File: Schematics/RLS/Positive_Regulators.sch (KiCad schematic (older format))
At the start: 4 parts

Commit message: Updated Regulator Circuits and Fixed Velleman Gain
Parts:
- removed U? (x2): AD5293, symbol AD5293
- added C21, C23, C25, C27, C29, C31, C? (x2): 10uF, symbol CP1
- added C22, C24, C26, C28, C30, C32: 0.1uF, symbol C
- added C33, C35: 1uF, symbol CP1
- added R?: 4.7K, symbol R
- added R?: 1K, symbol R
- added U8, U9: AD5293, symbol AD5293-RESCUE-RLS
- gave numbers to parts that had none: 2
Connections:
- net labels added: +15V, +5V, -15V, -15v, -V2, -V2_SHDN, AGND, MOSI, P_POT_CE, SCLK
- wire segments 0 -> 76
- no-connect marks 0 -> 3
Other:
- moved on the sheet: U10, U11

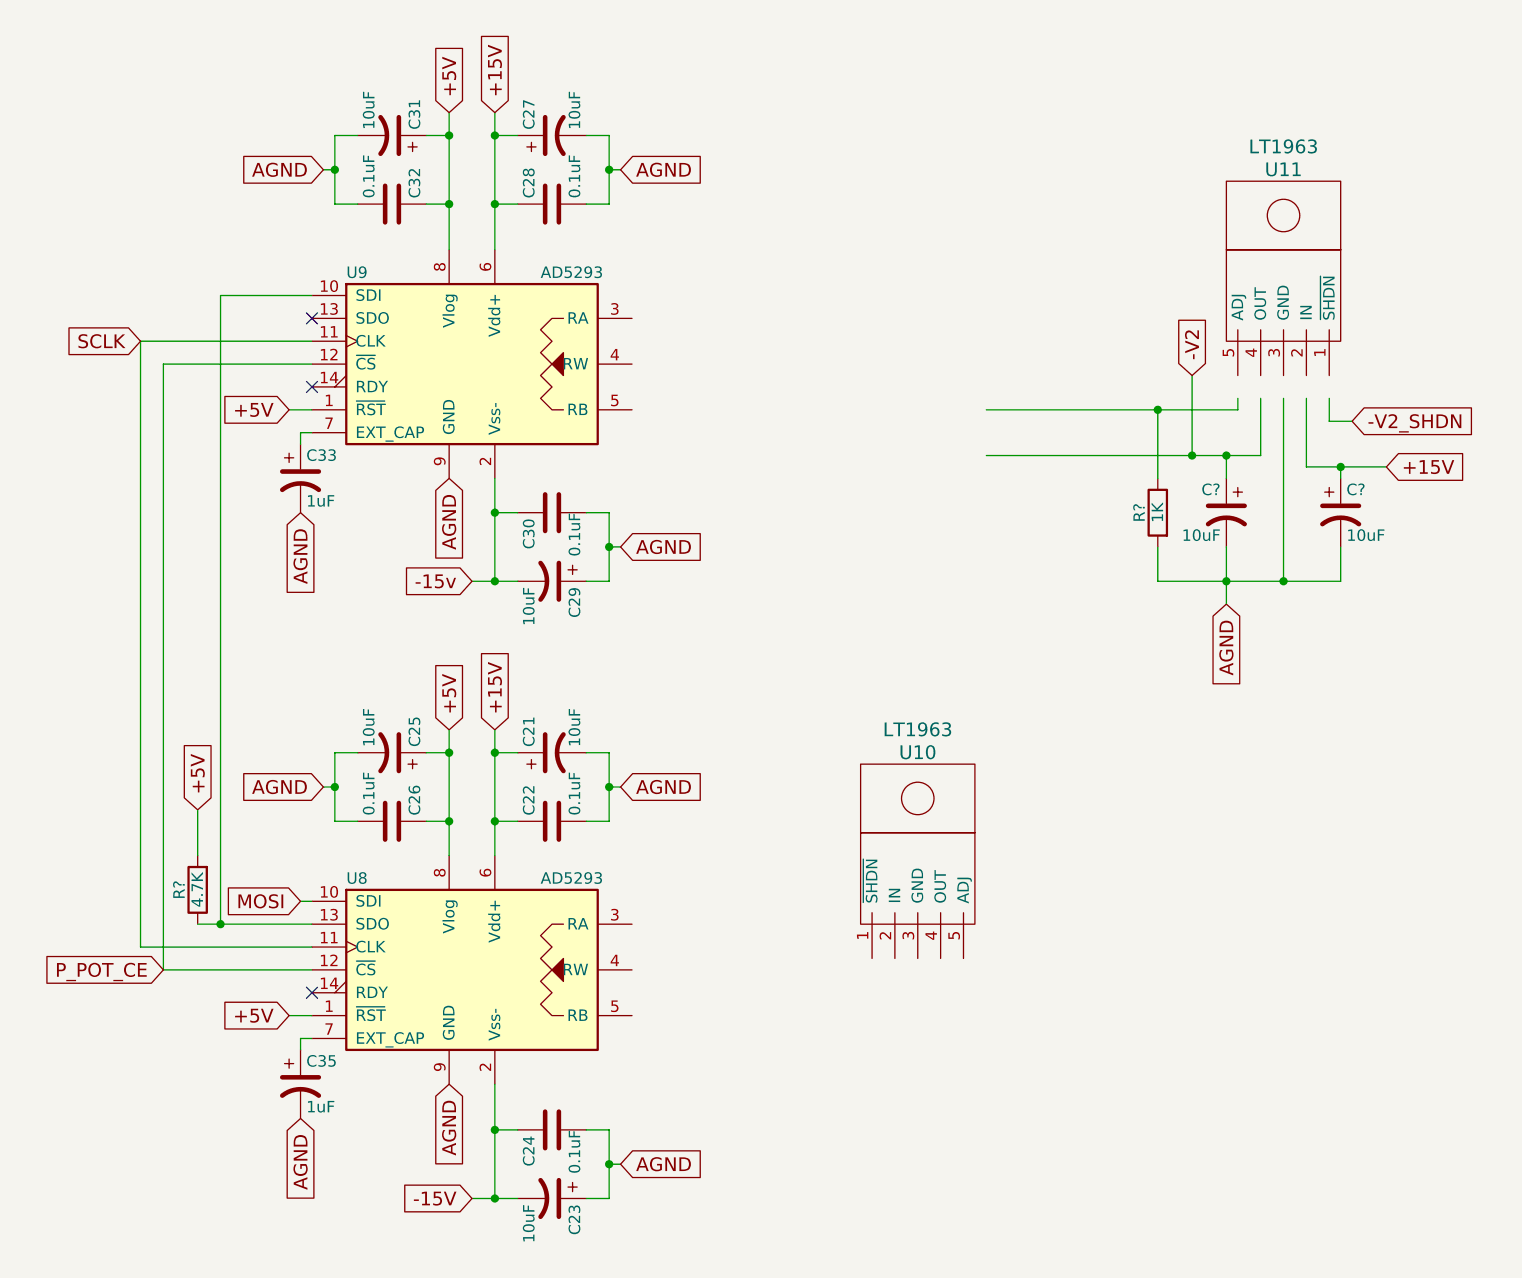
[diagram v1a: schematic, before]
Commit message: Updated Schematic (Almost Done)
Finished both variable regulator circuits, added connectors for LAs, added +/- 5 regulated circuit for DB +/- 5V (needs to be tested before PCB implementation), various renaming and labeling
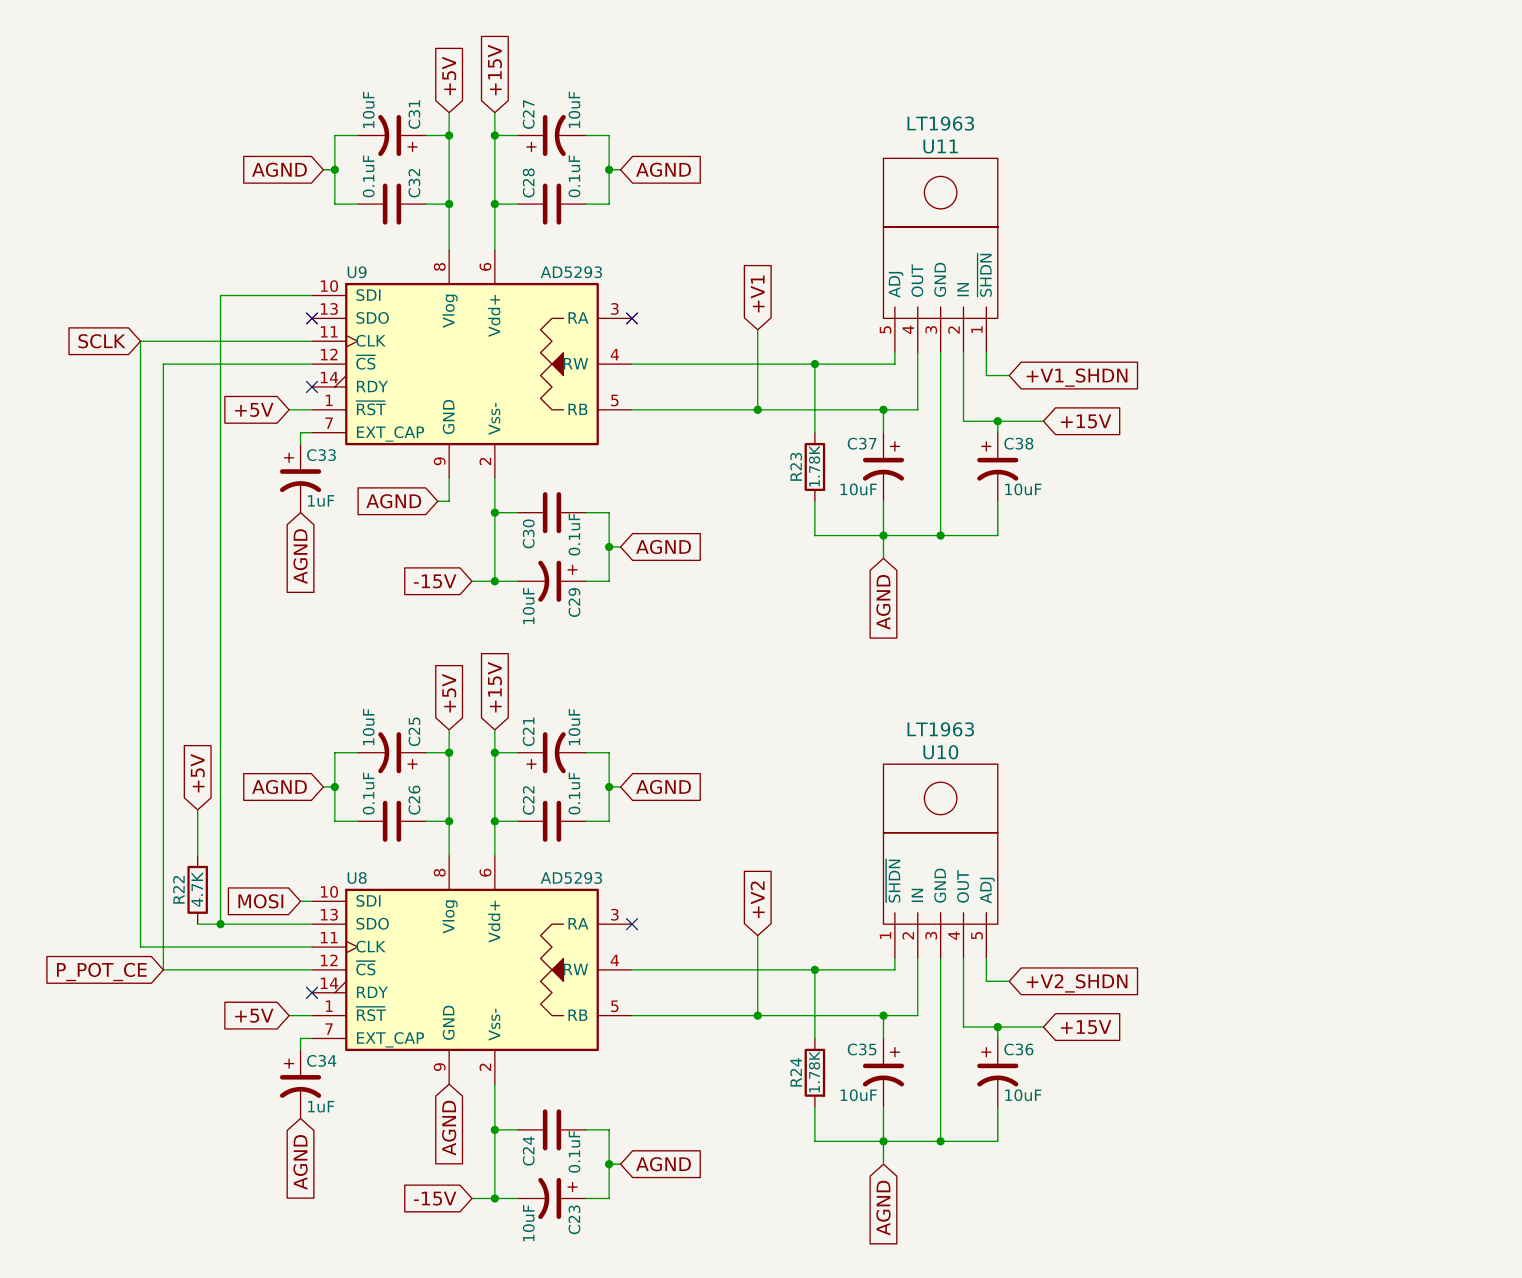
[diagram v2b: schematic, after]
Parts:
- added C35, C36: 10uF, symbol CP1
- added R24: 1.78K, symbol R
- R23: renamed from R?; value 1K -> 1.78K
- gave numbers to parts that had none: 3
- renumbered C35 to C34
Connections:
- net labels added: +V1, +V1_SHDN, +V2, +V2_SHDN
- net labels removed: -15v, -V2, -V2_SHDN
- wire segments 76 -> 95
- no-connect marks 3 -> 5
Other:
- moved on the sheet: C37, C38, R23, U10, U11

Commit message: Most Footprints Added
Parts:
- C21, C23, C25, C27, C29, C31, C33, C34, C35, C36, C37, C38: footprint (none) -> Capacitors_SMD:CP_Elec_4x5.3
- C22, C24, C26, C28, C30, C32: footprint (none) -> Capacitors_SMD:C_0603_HandSoldering
- R22: footprint (none) -> Resistors_SMD:R_0805_HandSoldering
- R23, R24: footprint (none) -> Resistors_SMD:R_1206_HandSoldering
- U10, U11: footprint (none) -> TO_SOT_Packages_THT:TO-220-5_Pentawatt_Multiwatt-5_Vertical_StaggeredType1
- U8, U9: footprint (none) -> SMD_Packages:SSOP-14
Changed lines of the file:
@@
 F 0 "U11" H 5250 2700 60  0000 C CNN
 F 1 "LT1963" H 5250 2800 60  0000 C CNN
-F 2 "" H 5250 2700 60  0001 C CNN
+F 2 "TO_SOT_Packages_THT:TO-220-5_Pentawatt_Multiwatt-5_Vertical_StaggeredType1" H 5250 2700 60  0001 C CNN
 F 3 "" H 5250 2700 60  0001 C CNN
 	1    5200 2200
@@
 F 0 "U10" H 5150 5350 60  0000 C CNN
 F 1 "LT1963" H 5150 5450 60  0000 C CNN
-F 2 "" H 5150 5350 60  0001 C CNN
+F 2 "TO_SOT_Packages_THT:TO-220-5_Pentawatt_Multiwatt-5_Vertical_StaggeredType1" H 5150 5350 60  0001 C CNN
 F 3 "" H 5150 5350 60  0001 C CNN
 	1    5100 4850
@@
 F 0 "U8" H 2550 5700 50  0000 L CNN
 F 1 "AD5293" H 3400 5700 50  0000 L CNN
-F 2 "" H 3100 5300 50  0001 C CNN
+F 2 "SMD_Packages:SSOP-14" H 3100 5300 50  0001 C CNN
 F 3 "" H 3100 5300 50  0001 C CNN
 	1    3100 5300
@@
 F 0 "U9" H 2550 3050 50  0000 L CNN
 F 1 "AD5293" H 3400 3050 50  0000 L CNN
-F 2 "" H 3100 2650 50  0001 C CNN
+F 2 "SMD_Packages:SSOP-14" H 3100 2650 50  0001 C CNN
 F 3 "" H 3100 2650 50  0001 C CNN
 	1    3100 2650
@@
 F 0 "C33" H 2375 3250 50  0000 L CNN
 F 1 "1uF" H 2375 3050 50  0000 L CNN
-F 2 "" H 2350 3150 50  0001 C CNN
+F 2 "Capacitors_SMD:CP_Elec_4x5.3" H 2350 3150 50  0001 C CNN
 F 3 "" H 2350 3150 50  0001 C CNN
 	1    2350 3150
@@
 F 0 "C34" H 2375 5900 50  0000 L CNN
 F 1 "1uF" H 2375 5700 50  0000 L CNN
-F 2 "" H 2350 5800 50  0001 C CNN
+F 2 "Capacitors_SMD:CP_Elec_4x5.3" H 2350 5800 50  0001 C CNN
 F 3 "" H 2350 5800 50  0001 C CNN
 	1    2350 5800
@@
 F 0 "C21" H 3475 4450 50  0000 L CNN
 F 1 "10uF" H 3475 4250 50  0000 L CNN
-F 2 "" H 3450 4350 50  0001 C CNN
+F 2 "Capacitors_SMD:CP_Elec_4x5.3" H 3450 4350 50  0001 C CNN
 F 3 "" H 3450 4350 50  0001 C CNN
 	1    3450 4350
@@
 F 0 "C22" H 3475 4750 50  0000 L CNN
 F 1 "0.1uF" H 3475 4550 50  0000 L CNN
-F 2 "" H 3488 4500 50  0001 C CNN
+F 2 "Capacitors_SMD:C_0603_HandSoldering" H 3488 4500 50  0001 C CNN
 F 3 "" H 3450 4650 50  0001 C CNN
 	1    3450 4650
@@
 F 0 "R22" V 1980 4950 50  0000 C CNN
 F 1 "4.7K" V 1900 4950 50  0000 C CNN
-F 2 "" V 1830 4950 50  0001 C CNN
+F 2 "Resistors_SMD:R_0805_HandSoldering" V 1830 4950 50  0001 C CNN
 F 3 "" H 1900 4950 50  0001 C CNN
 	1    1900 4950
@@
 F 0 "C25" H 2775 4450 50  0000 L CNN
 F 1 "10uF" H 2775 4250 50  0000 L CNN
-F 2 "" H 2750 4350 50  0001 C CNN
+F 2 "Capacitors_SMD:CP_Elec_4x5.3" H 2750 4350 50  0001 C CNN
 F 3 "" H 2750 4350 50  0001 C CNN
 	1    2750 4350
@@
 F 0 "C26" H 2775 4750 50  0000 L CNN
 F 1 "0.1uF" H 2775 4550 50  0000 L CNN
-F 2 "" H 2788 4500 50  0001 C CNN
+F 2 "Capacitors_SMD:C_0603_HandSoldering" H 2788 4500 50  0001 C CNN
 F 3 "" H 2750 4650 50  0001 C CNN
 	1    2750 4650
@@
 F 0 "C27" H 3475 1750 50  0000 L CNN
 F 1 "10uF" H 3475 1550 50  0000 L CNN
-F 2 "" H 3450 1650 50  0001 C CNN
+F 2 "Capacitors_SMD:CP_Elec_4x5.3" H 3450 1650 50  0001 C CNN
 F 3 "" H 3450 1650 50  0001 C CNN
 	1    3450 1650
@@
 F 0 "C28" H 3475 2050 50  0000 L CNN
 F 1 "0.1uF" H 3475 1850 50  0000 L CNN
-F 2 "" H 3488 1800 50  0001 C CNN
+F 2 "Capacitors_SMD:C_0603_HandSoldering" H 3488 1800 50  0001 C CNN
 F 3 "" H 3450 1950 50  0001 C CNN
 	1    3450 1950
@@
 F 0 "C32" H 2775 2050 50  0000 L CNN
 F 1 "0.1uF" H 2775 1850 50  0000 L CNN
-F 2 "" H 2788 1800 50  0001 C CNN
+F 2 "Capacitors_SMD:C_0603_HandSoldering" H 2788 1800 50  0001 C CNN
 F 3 "" H 2750 1950 50  0001 C CNN
 	1    2750 1950
@@
 F 0 "C29" H 3475 3700 50  0000 L CNN
 F 1 "10uF" H 3475 3500 50  0000 L CNN
-F 2 "" H 3450 3600 50  0001 C CNN
+F 2 "Capacitors_SMD:CP_Elec_4x5.3" H 3450 3600 50  0001 C CNN
 F 3 "" H 3450 3600 50  0001 C CNN
 	1    3450 3600
@@
 F 0 "C30" H 3475 3400 50  0000 L CNN
 F 1 "0.1uF" H 3450 3200 50  0000 L CNN
-F 2 "" H 3488 3150 50  0001 C CNN
+F 2 "Capacitors_SMD:C_0603_HandSoldering" H 3488 3150 50  0001 C CNN
 F 3 "" H 3450 3300 50  0001 C CNN
 	1    3450 3300
@@
 F 0 "C23" H 3475 6400 50  0000 L CNN
 F 1 "10uF" H 3475 6200 50  0000 L CNN
-F 2 "" H 3450 6300 50  0001 C CNN
+F 2 "Capacitors_SMD:CP_Elec_4x5.3" H 3450 6300 50  0001 C CNN
 F 3 "" H 3450 6300 50  0001 C CNN
 	1    3450 6300
@@
 F 0 "C24" H 3475 6100 50  0000 L CNN
 F 1 "0.1uF" H 3450 5900 50  0000 L CNN
-F 2 "" H 3488 5850 50  0001 C CNN
+F 2 "Capacitors_SMD:C_0603_HandSoldering" H 3488 5850 50  0001 C CNN
 F 3 "" H 3450 6000 50  0001 C CNN
 	1    3450 6000
@@
 F 0 "C31" H 2775 1750 50  0000 L CNN
 F 1 "10uF" H 2775 1550 50  0000 L CNN
-F 2 "" H 2750 1650 50  0001 C CNN
+F 2 "Capacitors_SMD:CP_Elec_4x5.3" H 2750 1650 50  0001 C CNN
 F 3 "" H 2750 1650 50  0001 C CNN
 	1    2750 1650
@@
 F 0 "R23" V 4680 3100 50  0000 C CNN
 F 1 "1.78K" V 4600 3100 47  0000 C CNN
-F 2 "" V 4530 3100 50  0001 C CNN
+F 2 "Resistors_SMD:R_1206_HandSoldering" V 4530 3100 50  0001 C CNN
 F 3 "" H 4600 3100 50  0001 C CNN
 	1    4600 3100
@@
 F 0 "C37" H 4925 3200 50  0000 L CNN
 F 1 "10uF" H 4925 3000 50  0000 L CNN
-F 2 "" H 4900 3100 50  0001 C CNN
+F 2 "Capacitors_SMD:CP_Elec_4x5.3" H 4900 3100 50  0001 C CNN
 F 3 "" H 4900 3100 50  0001 C CNN
 	1    4900 3100
@@
 F 0 "C38" H 5425 3200 50  0000 L CNN
 F 1 "10uF" H 5425 3000 50  0000 L CNN
-F 2 "" H 5400 3100 50  0001 C CNN
+F 2 "Capacitors_SMD:CP_Elec_4x5.3" H 5400 3100 50  0001 C CNN
 F 3 "" H 5400 3100 50  0001 C CNN
 	1    5400 3100
@@
 F 0 "R24" V 4680 5750 50  0000 C CNN
 F 1 "1.78K" V 4600 5750 47  0000 C CNN
-F 2 "" V 4530 5750 50  0001 C CNN
+F 2 "Resistors_SMD:R_1206_HandSoldering" V 4530 5750 50  0001 C CNN
 F 3 "" H 4600 5750 50  0001 C CNN
 	1    4600 5750
@@
 F 0 "C35" H 4925 5850 50  0000 L CNN
 F 1 "10uF" H 4925 5650 50  0000 L CNN
-F 2 "" H 4900 5750 50  0001 C CNN
+F 2 "Capacitors_SMD:CP_Elec_4x5.3" H 4900 5750 50  0001 C CNN
 F 3 "" H 4900 5750 50  0001 C CNN
 	1    4900 5750
@@
 F 0 "C36" H 5425 5850 50  0000 L CNN
 F 1 "10uF" H 5425 5650 50  0000 L CNN
-F 2 "" H 5400 5750 50  0001 C CNN
+F 2 "Capacitors_SMD:CP_Elec_4x5.3" H 5400 5750 50  0001 C CNN
 F 3 "" H 5400 5750 50  0001 C CNN
 	1    5400 5750
